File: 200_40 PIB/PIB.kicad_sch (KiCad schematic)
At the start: 35 parts, among them J1 Igniter, J10 TC2, J2 Rogowski, J3 PIB Interface, J6 Main Disch, J7 Heater 1, J8 Heater 1, J9 TC1, Q1 3300V, Q3 VO3120, Q6 AO3400A, Q7 AO3400A, U1 ACS37042KLHBLT-030B3, U10 TLP3543, U14 VO618A, U2 STM32G431KBTx, U3 BDJ2FC0WEFJ

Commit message: intermediate pib work, add history to gitignore
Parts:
- removed U2: STM32G431KBTx, Package_QFP:LQFP-32_7x7mm_P0.8mm, symbol MCU_ST_STM32G4:STM32G431KBTx
- added U11: STM32G431KBTx, Package_QFP:LQFP-32_7x7mm_P0.8mm, symbol MCU_ST_STM32G4:STM32G431KBTx
- J3: footprint (none) -> Connector_Harwin:Harwin_Gecko_G125-MS12605M2P_2x13_P1.25mm_Vertical
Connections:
- net +3.3V: now also U11.1 (VDD), U11.17 (VDD)
- net AREF: now also U11.15 (VDDA)
- net Discharge Supply/EN: now also U11.3 (PF1)
- net Discharge Supply/V_CTRL: now also U11.27 (PB4)
- net FIRE: now also U11.31 (PB8)
- net GNDPWR: now also U11.16 (VSS), U11.32 (VSS)
- net GNDREF: now also U11.14 (VSSA)
- net I_IG: now also U11.10 (PA5)
- net Igniter Supply/EN: now also U11.28 (PB5)
- net Igniter Supply/V_CTRL: now also U11.2 (PF0)
- net RESET: now also U11.4 (PG10)
- net SCL: now also U11.25 (PA15)
- net SDA: now also U11.30 (PB7)
- net SWDCLK: now also U11.24 (PA14)
- net SWDIO: now also U11.23 (PA13)
- net USART2_RX: now also U11.8 (PA3)
- net USART2_TX: now also U11.7 (PA2)
- net V_IG: now also U11.6 (PA1)
- net V_MAIN: now also U11.5 (PA0)
- net Valve Driver/LHD1: now also U11.18 (PA8)
- net Valve Driver/LHL1: now also U11.19 (PA9)
- net Valve Driver/LHL2: now also U11.20 (PA10)
- net Valve Driver/LHL3: now also U11.21 (PA11)
- net Valve Driver/LHL4: now also U11.22 (PA12)
- net at J9.1 (Pin_1), R7.1: now also U11.11 (PA6)
- net at Q6.2 (G): now also U11.13 (PB0)
- net at J10.1 (Pin_1), R8.1: now also U11.12 (PA7)
- net at J2.1 (In): now also U11.9 (PA4)
- net at Q7.2 (G): now also U11.26 (PB3)
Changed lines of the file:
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@@
 	)
 	(symbol
+		(lib_id "MCU_ST_STM32G4:STM32G431KBTx")
+		(at 80.01 74.93 0)
+		(unit 1)
+		(body_style 1)
+		(exclude_from_sim no)
+		(in_bom yes)
+		(on_board yes)
+		(in_pos_files yes)
+		(dnp no)
+		(fields_autoplaced yes)
+		(property "Reference" "U11"
+			(at 84.6933 100.33 0)
+			(show_name no)
+			(do_not_autoplace no)
+			(effects
+				(font
+					(size 1.27 1.27)
+				)
+				(justify left)
+			)
+		)
+		(property "Value" "STM32G431KBTx"
+			(at 84.6933 102.87 0)
+			(show_name no)
+			(do_not_autoplace no)
+			(effects
+				(font
+					(size 1.27 1.27)
+				)
+				(justify left)
+			)
+		)
+		(property "Footprint" "Package_QFP:LQFP-32_7x7mm_P0.8mm"
+			(at 69.85 97.79 0)
+			(hide yes)
+			(show_name no)
+			(do_not_autoplace no)
+			(effects
+				(font
+					(size 1.27 1.27)
+				)
+				(justify right)
+			)
+		)
+		(property "Datasheet" "https://www.st.com/resource/en/datasheet/stm32g431kb.pdf"
+			(at 80.01 74.93 0)
+			(hide yes)
+			(show_name no)
+			(do_not_autoplace no)
+			(effects
+				(font
+					(size 1.27 1.27)
+				)
+			)
+		)
+		(property "Description" "STMicroelectronics Arm Cortex-M4 MCU, 128KB flash, 32KB RAM, 170 MHz, 1.71-3.6V, 26 GPIO, LQFP32"
+			(at 80.01 74.93 0)
+			(hide yes)
+			(show_name no)
+			(do_not_autoplace no)
+			(effects
+				(font
+					(size 1.27 1.27)
+				)
+			)
+		)
+		(pin "9"
+		)
+		(pin "11"
+		)
+		(pin "10"
+		)
+		(pin "13"
+		)
+		(pin "2"
+		)
+		(pin "12"
+		)
+		(pin "20"
+		)
+		(pin "24"
+		)
+		(pin "29"
+		)
+		(pin "17"
+		)
+		(pin "18"
+		)
+		(pin "21"
+		)
+		(pin "22"
+		)
+		(pin "23"
+		)
+		(pin "16"
+		)
+		(pin "31"
+		)
+		(pin "8"
+		)
+		(pin "28"
+		)
+		(pin "15"
+		)
+		(pin "27"
+		)
+		(pin "32"
+		)
+		(pin "26"
+		)
+		(pin "25"
+		)
+		(pin "14"
+		)
+		(pin "30"
+		)
+		(pin "19"
+		)
+		(pin "3"
+		)
+		(pin "4"
+		)
+		(pin "5"
+		)
+		(pin "1"
+		)
+		(pin "6"
+		)
+		(pin "7"
+		)
+		(instances
+			(project "PIB"
+				(path "/2bb2e4a1-de70-477a-a246-143db0a21e08"
+					(reference "U11")
+					(unit 1)
+				)
+			)
+		)
+	)
+	(symbol
 		(lib_id "Device:C")
 		(at 48.26 186.69 0)
@@
 			)
 		)
-		(property "Footprint" ""
+		(property "Footprint" "Connector_Harwin:Harwin_Gecko_G125-MS12605M2P_2x13_P1.25mm_Vertical"
 			(at 77.47 156.21 0)
 			(hide yes)
@@
 					(unit 1)
 				)
-			)
-		)
-	)
-	(symbol
-		(lib_id "MCU_ST_STM32G4:STM32G431KBTx")
-		(at 80.01 74.93 0)
-		(unit 1)
-		(body_style 1)
-		(exclude_from_sim no)
-		(in_bom yes)
-		(on_board yes)
-		(in_pos_files yes)
-		(dnp no)
-		(fields_autoplaced yes)
-		(property "Reference" "U2"
-			(at 84.6933 100.33 0)
-			(show_name no)
-			(do_not_autoplace no)
-			(effects
-				(font
-					(size 1.27 1.27)
-				)
-				(justify left)
-			)
-		)
-		(property "Value" "STM32G431KBTx"
-			(at 84.6933 102.87 0)
-			(show_name no)
-			(do_not_autoplace no)
-			(effects
-				(font
-					(size 1.27 1.27)
-				)
-				(justify left)
-			)
-		)
-		(property "Footprint" "Package_QFP:LQFP-32_7x7mm_P0.8mm"
-			(at 69.85 97.79 0)
-			(hide yes)
-			(show_name no)
-			(do_not_autoplace no)
-			(effects
-				(font
-					(size 1.27 1.27)
-				)
-				(justify right)
-			)
-		)
-		(property "Datasheet" "https://www.st.com/resource/en/datasheet/stm32g431kb.pdf"
-			(at 80.01 74.93 0)
-			(hide yes)
-			(show_name no)
-			(do_not_autoplace no)
-			(effects
-				(font
-					(size 1.27 1.27)
-				)
-			)
-		)
-		(property "Description" "STMicroelectronics Arm Cortex-M4 MCU, 128KB flash, 32KB RAM, 170 MHz, 1.71-3.6V, 26 GPIO, LQFP32"
-			(at 80.01 74.93 0)
-			(hide yes)
-			(show_name no)
-			(do_not_autoplace no)
-			(effects
-				(font
-					(size 1.27 1.27)
-				)
-			)
-		)
-		(pin "15"
-		)
-		(pin "1"
-		)
-		(pin "4"
-		)
-		(pin "9"
-		)
-		(pin "14"
-		)
-		(pin "13"
-		)
-		(pin "5"
-		)
-		(pin "7"
-		)
-		(pin "24"
-		)
-		(pin "6"
-		)
-		(pin "8"
-		)
-		(pin "10"
-		)
-		(pin "11"
-		)
-		(pin "18"
-		)
-		(pin "20"
-		)
-		(pin "27"
-		)
-		(pin "2"
-		)
-		(pin "12"
-		)
-		(pin "28"
-		)
-		(pin "31"
-		)
-		(pin "19"
-		)
-		(pin "21"
-		)
-		(pin "32"
-		)
-		(pin "3"
-		)
-		(pin "17"
-		)
-		(pin "30"
-		)
-		(pin "26"
-		)
-		(pin "16"
-		)
-		(pin "22"
-		)
-		(pin "23"
-		)
-		(pin "25"
-		)
-		(pin "29"
-		)
-		(instances
-			(project "PIB"
-				(path "/2bb2e4a1-de70-477a-a246-143db0a21e08"
-					(reference "U2")
-					(unit 1)
-				)

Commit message: pretty pib that doesnt work
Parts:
- removed C1: 0.47uF, Capacitor_THT:C_Rect_L41.5mm_W13.0mm_P37.50mm_MKS4, symbol Device:C
- removed Q6, Q7: AO3400A, digikey-footprints:SOT-23-3, symbol Simulation_SPICE:NMOS
- added Q8, Q9: IRF7403, Package_SO:SOIC-8_3.9x4.9mm_P1.27mm, symbol Transistor_FET:IRF7403
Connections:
- net GNDPWR: now also Q8.1 (S), Q8.2 (S), Q8.3 (S), Q9.1 (S), Q9.2 (S), Q9.3 (S)
- net at U11.13 (PB0): now also Q8.4 (G)
- net at U11.26 (PB3): now also Q9.4 (G)
- net at J7.2 (Pin_2): now also Q8.5 (D), Q8.6 (D), Q8.7 (D), Q8.8 (D)
- net at J8.2 (Pin_2): now also Q9.5 (D), Q9.6 (D), Q9.7 (D), Q9.8 (D)

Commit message: remove converters from PIB. WIP, do not check out
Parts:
- removed C6: 10nF, symbol Device:C
- removed J1: Igniter, symbol Connector:Conn_Coaxial_Power
- removed J6: Main Disch, symbol Connector:Conn_01x02_Pin
- removed Q1: 3300V, Package_TO_SOT_THT:TO-247-4_Horizontal_TabDown, symbol Simulation_SPICE:NMOS
- removed Q3: VO3120, DIP_3120_VIS, symbol PIB_Symbol_Library:VO3120
- removed R1: 100k, symbol Device:R
- removed R10, R11, R3: 10M, symbol Device:R
- removed R12, R4: 10k, symbol Device:R
- removed R2: 300k, symbol Device:R
- removed R9: 20k, symbol Device:R
- removed U1: ACS37042KLHBLT-030B3, Package_TO_SOT_SMD:SOT-23-5_HandSoldering, symbol 0_PAY_Symbol_Library:ACS37042KLHBLT-030B3
- removed U14: VO618A, VO618A:DIP762W50P254L458H480Q4, symbol 0_PAY_Symbol_Library:VO618A
- added J1: M80-5100442, Package_LCC:PLCC-84_29.3x29.3mm_P1.27mm, symbol Connector_Generic:Conn_02x02_Top_Bottom
- J3: value PIB Interface -> G125-MS12605M2P
- Q8, Q9: value IRF7403 -> IRF7832
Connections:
- net +12V: now also C2.1, C3.1, C4.1, FB1.1, U10.5, U3.5 (EN), U3.8 (VCC)
- net +3.3V: now also C2.2, C5.2, F3.2, J3.4 (Pin_4), J3.5 (Pin_5), Q8.1 (S), Q8.2 (S), Q8.3 (S), Q9.1 (S), Q9.2 (S), Q9.3 (S), U10.2, U10.4, U10.6, U11.16 (VSS), U11.32 (VSS), U3.3 (GND), U3.9 (GND); no longer J3.12 (Pin_12)
- net +5V: now also J3.12 (Pin_12), J3.13 (Pin_13)
- net AREF: no longer C3.1, C4.1, FB1.1
- net FIRE: no longer J3.25 (Pin_25)
- net GNDREF: no longer J3.26 (Pin_26)
- net SCL: no longer J3.21 (Pin_21)
- net SDA: no longer J3.22 (Pin_22)
- net SWDCLK: no longer J3.24 (Pin_24)
- net SWDIO: no longer J3.23 (Pin_23)
- net USART2_RX: no longer J3.20 (Pin_20)
- net USART2_TX: no longer J3.19 (Pin_19)
- net BAT_HOT: now reaches J3.1 (Pin_1)
- net BAT_HOT: now also J3.2 (Pin_2), J3.3 (Pin_3)
- net GND: now reaches J3.14 (Pin_14)
- net GND: now also J3.15 (Pin_15), J3.16 (Pin_16), J3.17 (Pin_17), J3.18 (Pin_18), J3.19 (Pin_19), J3.25 (Pin_25), J3.26 (Pin_26), J1.3 (Pin_3), J1.4 (Pin_4)
- net EXT_SPI_MISO: now reaches J3.6 (Pin_6)
- net EXT_SPI_MOSI: now reaches J3.7 (Pin_7)
- net EXT_SPI_SCK: now reaches J3.8 (Pin_8)
- net EXT_SPI_~{CS}: now reaches J3.9 (Pin_9)
- net Discharge Supply/EN: no longer names the net of U11.3 (PF1)
- net Discharge Supply/V_CTRL: no longer names the net of U11.27 (PB4)
- removed net GNDPWR: C2.2, C5.2, J3.13 (Pin_13), Q8.1 (S), Q8.2 (S), Q8.3 (S), Q9.1 (S), Q9.2 (S), Q9.3 (S), U10.2, U11.16 (VSS), U11.32 (VSS), U3.3 (GND), U3.9 (GND)
- net Igniter Supply/EN: no longer names the net of U11.28 (PB5)
- net Igniter Supply/V_CTRL: no longer names the net of U11.2 (PF0)
- new net 12V_GSE_1: J1.1 (Pin_1)
- new net 12V_GSE_2: J1.2 (Pin_2)
- new net ARM/~{SAFE}: J3.24 (Pin_24)
- new net DRDY: J3.23 (Pin_23)
- new net EXT_I2C_SCL: J3.20 (Pin_20)
- new net EXT_I2C_SDA: J3.21 (Pin_21)
- new net IGNITER: J3.22 (Pin_22)
- now unconnected: J3.11 (Pin_11)
- no-connect marks 0 -> 2
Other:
- removed sheet Discharge Supply
- removed sheet Igniter Supply
- note added: "CDH"
- note added: "Connectors"
- note added: "GSE TANK FILL"
- note removed: "Power Conditioning"
- moved on the sheet: C2, C3, C4, C5, F3, FB1, J10, J2, J3, J7, J8, J9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

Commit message: arhutr
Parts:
- added C1, C6: 10uF, Capacitor_SMD:C_0805_2012Metric, symbol Device:C
- added R1: 100K, Resistor_SMD:R_0402_1005Metric, symbol Device:R
- added R2: 1K, Resistor_SMD:R_0402_1005Metric, symbol Device:R
- added U1: LT3065EDDPBF, 0_PAY_Footprint_Library:DFN-10_DD, symbol LT3065EDDPBF:LT3065EDDPBF
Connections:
- net BAT_HOT: now also C1.1, R1.1, U1.1 (IN), U1.2 (IN), U1.3 (*SHDN)
- net GND: now also C1.2, C6.2, R2.1, U1.11 (GND)
- new net: R1.2, U1.4 (PWRGD)
- new net: R2.2, U1.5 (IMAX)
- new net 12V: C6.1, U1.10 (OUT), U1.9 (OUT)

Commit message: john.
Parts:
- removed C2: 1uF, symbol Device:C
- removed C3, C5: 4.7uF, symbol Device:C
- removed C4: 100nF, symbol Device:C
- removed F3: Polyfuse, symbol Device:Polyfuse
- removed FB1: FerriteBead, symbol Device:FerriteBead
- removed U10: TLP3543, Package_DIP:DIP-6_W7.62mm, symbol Relay_SolidState:TLP3543
- removed U3: BDJ2FC0WEFJ, Package_SO:HTSOP-8-1EP_3.9x4.9mm_P1.27mm_EP2.4x3.2mm, symbol Regulator_Linear:BDJ2FC0WEFJ
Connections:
- net +3.3V: no longer Q8.1 (S), Q8.2 (S), Q8.3 (S), Q9.1 (S), Q9.2 (S), Q9.3 (S), U11.16 (VSS), U11.32 (VSS)
- net 12V_GSE_1 renamed 12V_GSE
- net 12V_GSE_2 renamed OPEN/~{CLOSE}
- new net GNDPWR: Q8.1 (S), Q8.2 (S), Q8.3 (S), Q9.1 (S), Q9.2 (S), Q9.3 (S), U11.16 (VSS), U11.32 (VSS)

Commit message: .nhoj
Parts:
- added C2: 10nF, symbol Device:C
- added J11: NTC1, symbol Connector:Conn_01x02_Pin
- added R3: 22K, Resistor_SMD:R_0402_1005Metric, symbol Device:R
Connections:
- net GND: now also C2.2, J11.2 (Pin_2)
- new net TANK_TEMP_1: C2.1, J11.1 (Pin_1), R3.1
- new net VDDA: R3.2

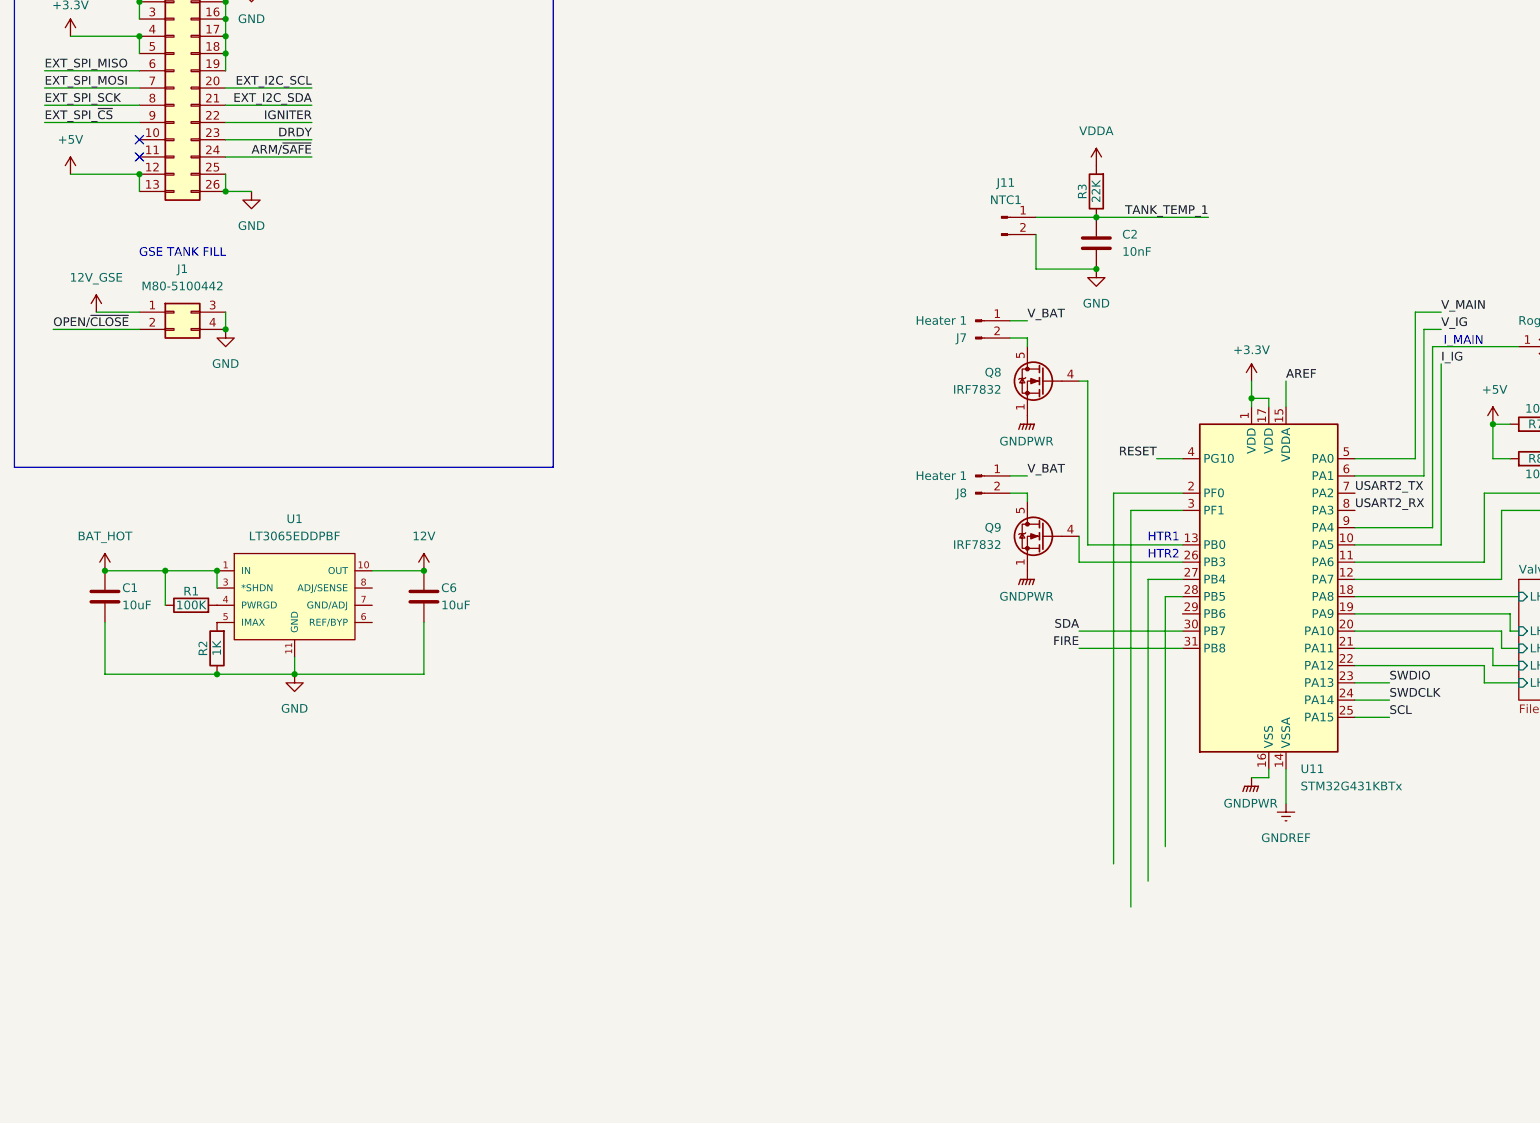
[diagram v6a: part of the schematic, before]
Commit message: changed to CBT, added 2 tank and 1 frit thermistor, flow sensor picoblade
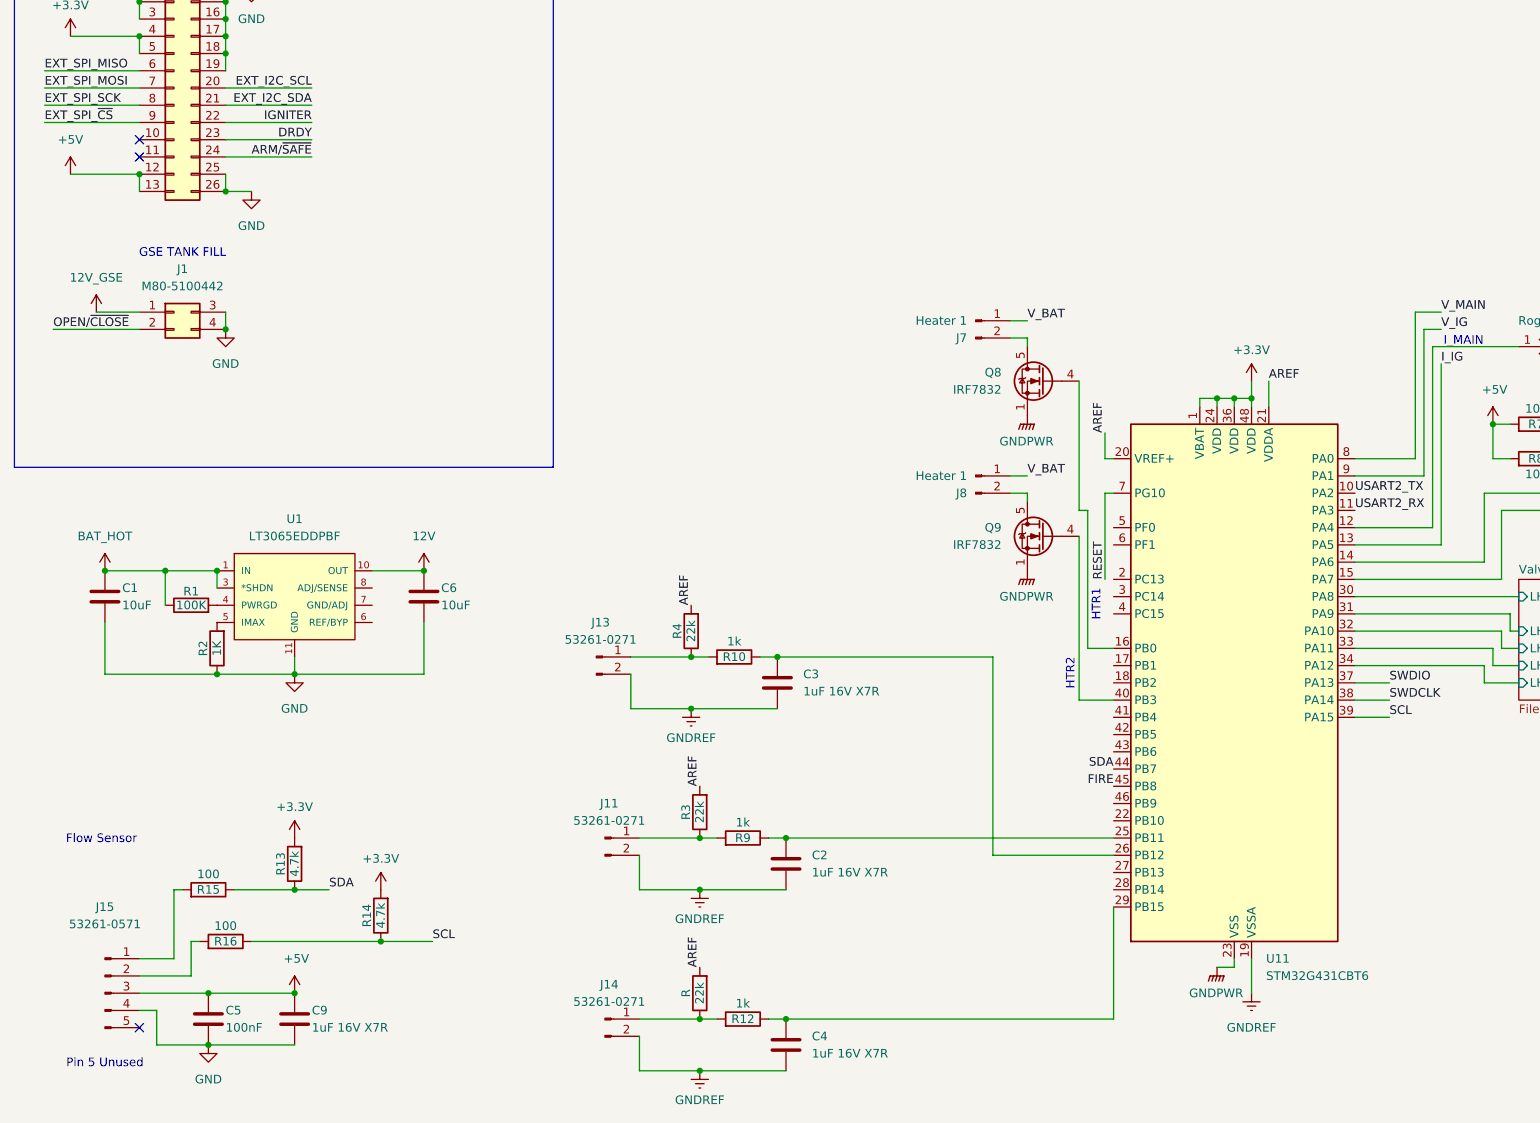
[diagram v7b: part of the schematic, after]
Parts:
- added C3, C4, C9: 1uF 16V X7R, Capacitor_SMD:C_0603_1608Metric, symbol Device:C
- added C5: 100nF, Capacitor_SMD:C_0402_1005Metric, symbol Device:C
- added J13, J14: 53261-0271, Connector_Molex:Molex_PicoBlade_53261-0271_1x02-1MP_P1.25mm_Horizontal, symbol Connector:Conn_01x02_Pin
- added J15: 53261-0571, Connector_Molex:Molex_PicoBlade_53261-0571_1x05-1MP_P1.25mm_Horizontal, symbol Connector:Conn_01x05_Pin
- added R, R4: 22k, Resistor_SMD:R_0402_1005Metric, symbol Device:R
- added R10, R12, R9: 1k, Resistor_SMD:R_0402_1005Metric, symbol Device:R
- added R13, R14: 4.7k, Resistor_SMD:R_0402_1005Metric, symbol Device:R
- added R15, R16: 100, Resistor_SMD:R_0402_1005Metric, symbol Device:R
- C2: value 10nF -> 1uF 16V X7R; footprint (none) -> Capacitor_SMD:C_0603_1608Metric
- J11: value NTC1 -> 53261-0271; footprint (none) -> Connector_Molex:Molex_PicoBlade_53261-0271_1x02-1MP_P1.25mm_Horizontal
- R3: value 22K -> 22k; Tolerance (none) -> 0.1%, 25ppm/C
- U11: value STM32G431KBTx -> STM32G431CBT6; footprint Package_QFP:LQFP-32_7x7mm_P0.8mm -> Package_QFP:LQFP-48_7x7mm_P0.5mm; symbol MCU_ST_STM32G4:STM32G431KBTx -> MCU_ST_STM32G4:STM32G431CBTx
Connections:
- net VDDA is gone; now on net AREF: R3.2
- net +3.3V: now also U11.24 (VDD), U11.36 (VDD), U11.48 (VDD), R13.2, R14.2; no longer U11.17 (VDD)
- net +5V: now also C5.1, C9.1, J15.3 (Pin_3)
- net AREF: now also U11.20 (VREF+), U11.21 (VDDA), R.2, R4.2; no longer U11.15 (VDDA)
- net FIRE: now also U11.45 (PB8); no longer U11.31 (PB8)
- net GND: now also C5.2, C9.2, J15.4 (Pin_4); no longer C2.2, J11.2 (Pin_2)
- net GNDPWR: now also U11.23 (VSS), U11.35 (VSS), U11.47 (VSS); no longer U11.16 (VSS), U11.32 (VSS)
- net GNDREF: now also C2.2, J11.2 (Pin_2), U11.19 (VSSA), C3.2, C4.2, J13.2 (Pin_2), J14.2 (Pin_2); no longer U11.14 (VSSA)
- net I_IG: now also U11.13 (PA5); no longer U11.10 (PA5)
- net RESET: now also U11.7 (PG10); no longer U11.4 (PG10)
- net SCL: now also U11.39 (PA15), R14.1, R16.1; no longer U11.25 (PA15)
- net SDA: now also U11.44 (PB7), R13.1, R15.1; no longer U11.30 (PB7)
- net SWDCLK: now also U11.38 (PA14); no longer U11.24 (PA14)
- net SWDIO: now also U11.37 (PA13); no longer U11.23 (PA13)
- net USART2_RX: now also U11.11 (PA3); no longer U11.8 (PA3)
- net USART2_TX: now also U11.10 (PA2); no longer U11.7 (PA2)
- net V_IG: now also U11.9 (PA1); no longer U11.6 (PA1)
- net V_MAIN: now also U11.8 (PA0); no longer U11.5 (PA0)
- net Valve Driver/LHD1: now also U11.30 (PA8); no longer U11.18 (PA8)
- net Valve Driver/LHL1: now also U11.31 (PA9); no longer U11.19 (PA9)
- net Valve Driver/LHL2: now also U11.32 (PA10); no longer U11.20 (PA10)
- net Valve Driver/LHL3: now also U11.33 (PA11); no longer U11.21 (PA11)
- net Valve Driver/LHL4: now also U11.34 (PA12); no longer U11.22 (PA12)
- net at J9.1 (Pin_1), R7.1: now also U11.14 (PA6); no longer U11.11 (PA6)
- net at J10.1 (Pin_1), R8.1: now also U11.15 (PA7); no longer U11.12 (PA7)
- net at Q8.4 (G): now also U11.16 (PB0); no longer U11.13 (PB0)
- net at U11.26 (PB12): now also C3.1, R10.1; no longer Q9.4 (G)
- net at U11.29 (PB15): now also C4.1, R12.1
- net at J2.1 (In): now also U11.12 (PA4); no longer U11.9 (PA4)
- net TANK_TEMP_1: no longer names the net of J11.1 (Pin_1), R3.1
- net TANK_TEMP_1: now also R9.2; no longer C2.1
- new net: C2.1, R9.1, U11.25 (PB11)
- new net: Q9.4 (G), U11.40 (PB3)
- new net: J15.1 (Pin_1), R15.2
- new net: J15.2 (Pin_2), R16.2
- new net: J13.1 (Pin_1), R10.2, R4.1
- new net: J14.1 (Pin_1), R.1, R12.2
- no-connect marks 2 -> 3
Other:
- note added: "Flow Sensor"
- note added: "Pin 5 Unused"
- moved on the sheet: C2, J11, R3
